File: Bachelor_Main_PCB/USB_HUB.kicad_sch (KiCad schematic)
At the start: 15 parts, among them J11 M20-9990245, U6 USB2514B-I/M2

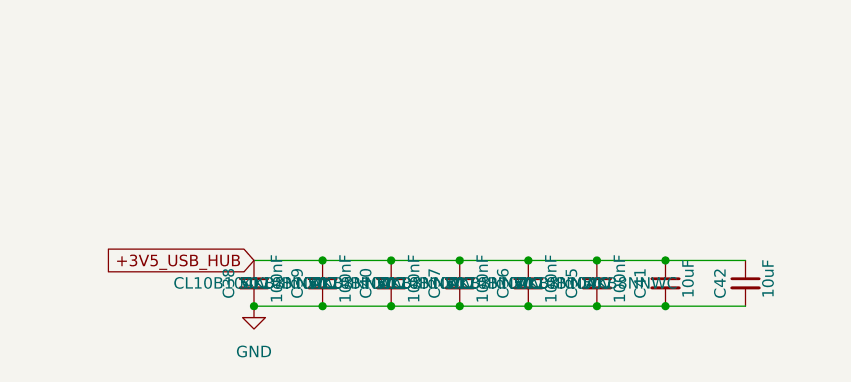
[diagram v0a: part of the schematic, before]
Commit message: Add pulldown to power switch mosfets
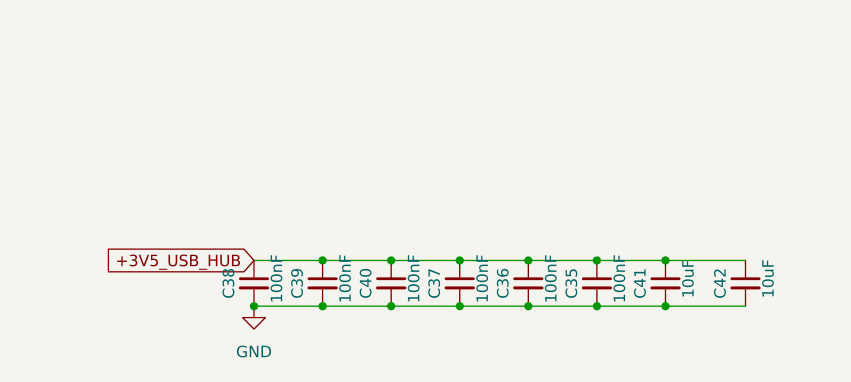
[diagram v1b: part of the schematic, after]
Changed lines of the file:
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@@
 					(size 1.27 1.27)
 				)
+				(hide yes)
 			)
 		)
@@
 					(size 1.27 1.27)
 				)
+				(hide yes)
 			)
 		)
@@
 					(size 1.27 1.27)
 				)
+				(hide yes)
 			)
 		)
@@
 					(size 1.27 1.27)
 				)
+				(hide yes)
 			)
 		)
@@
 					(size 1.27 1.27)
 				)
+				(hide yes)
 			)
 		)
@@
 					(size 1.27 1.27)
 				)
+				(hide yes)
 			)
 		)
@@
 					(size 1.27 1.27)
 				)
+				(hide yes)
 			)
 		)
@@
 					(size 1.27 1.27)
 				)
+				(hide yes)
 			)
 		)
@@
 					(size 1.27 1.27)
 				)
+				(hide yes)
 			)
 		)
@@
 					(size 1.27 1.27)
 				)
+				(hide yes)
 			)
 		)
@@
 					(size 1.27 1.27)
 				)
+				(hide yes)
 			)
 		)
@@
 					(size 1.27 1.27)
 				)
-			)
-		)
+				(hide yes)
+			)
+		)

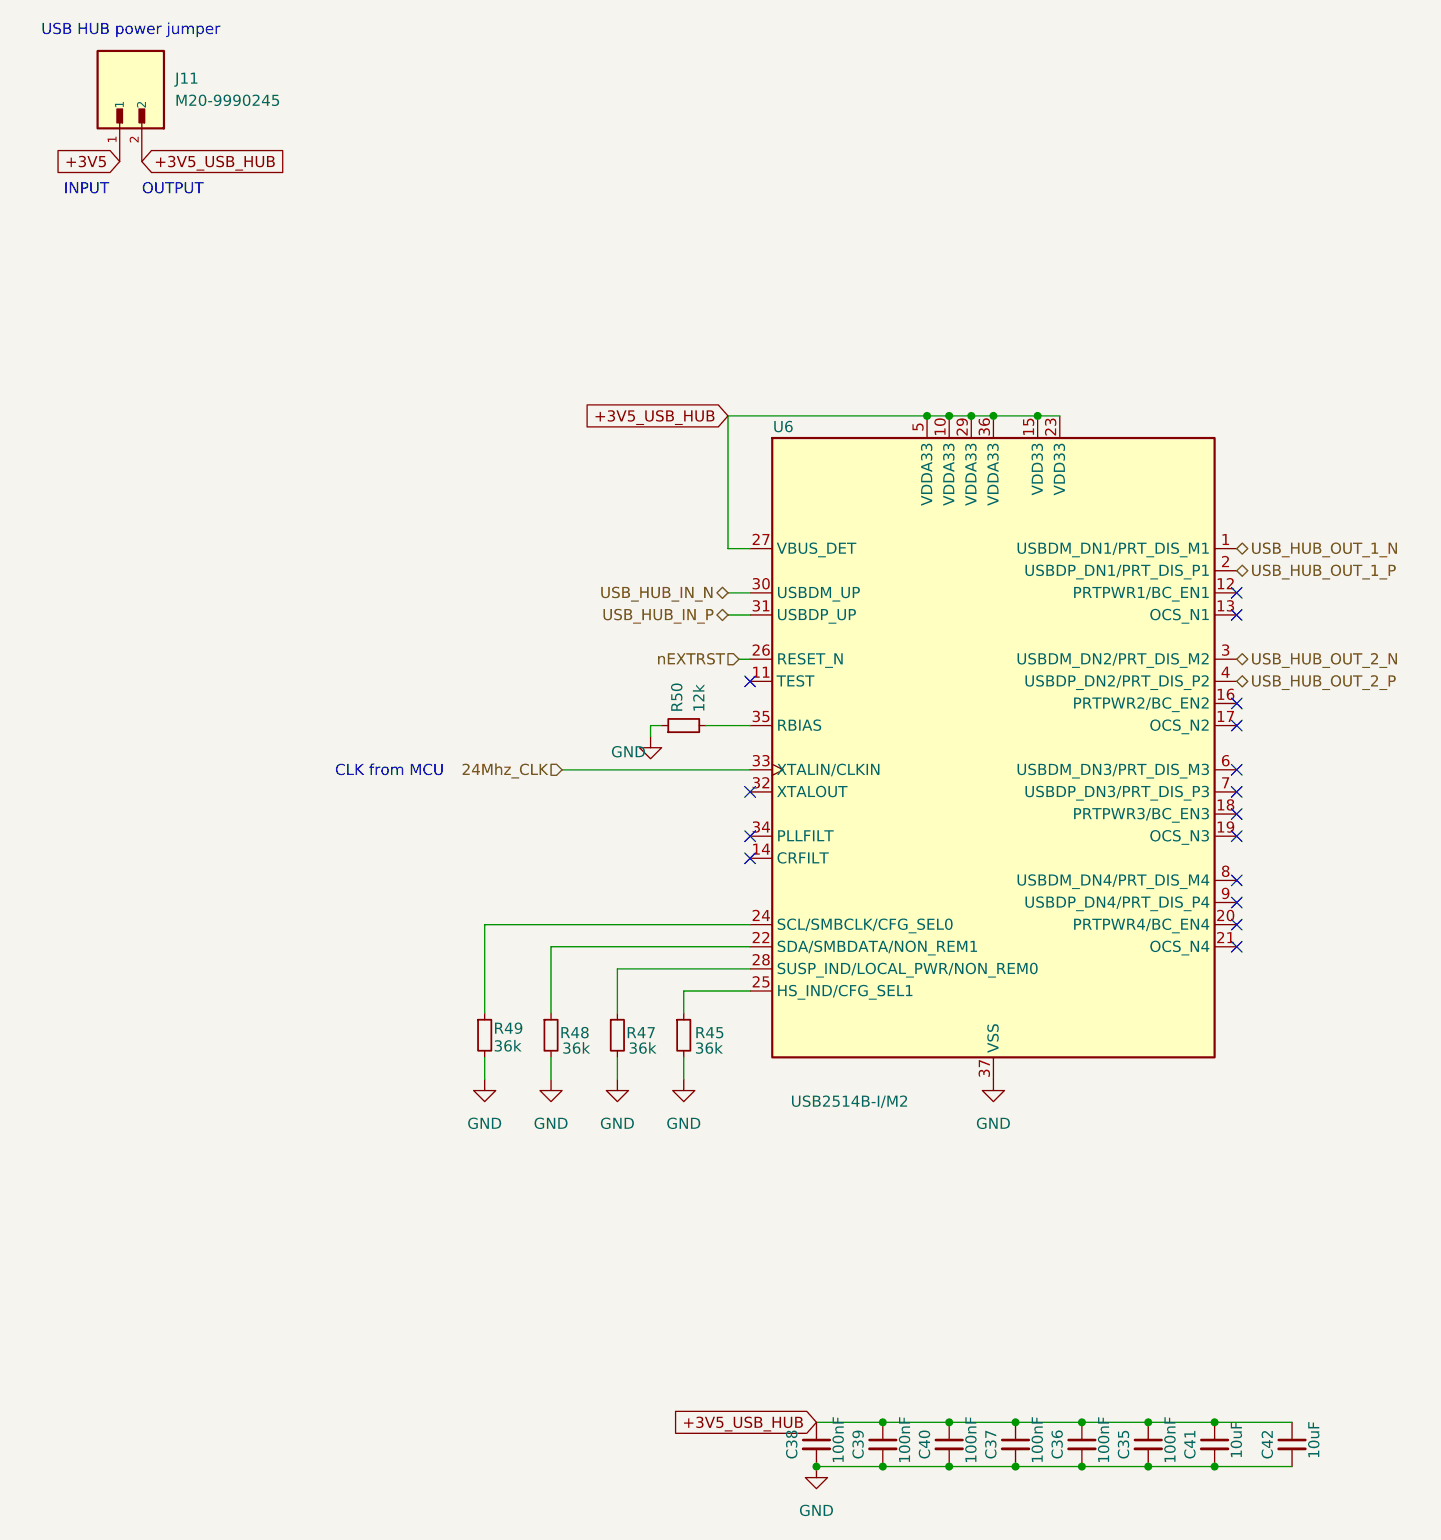
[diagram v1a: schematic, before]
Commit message: Fixed DRC, footprints and power flags and no-connect flags
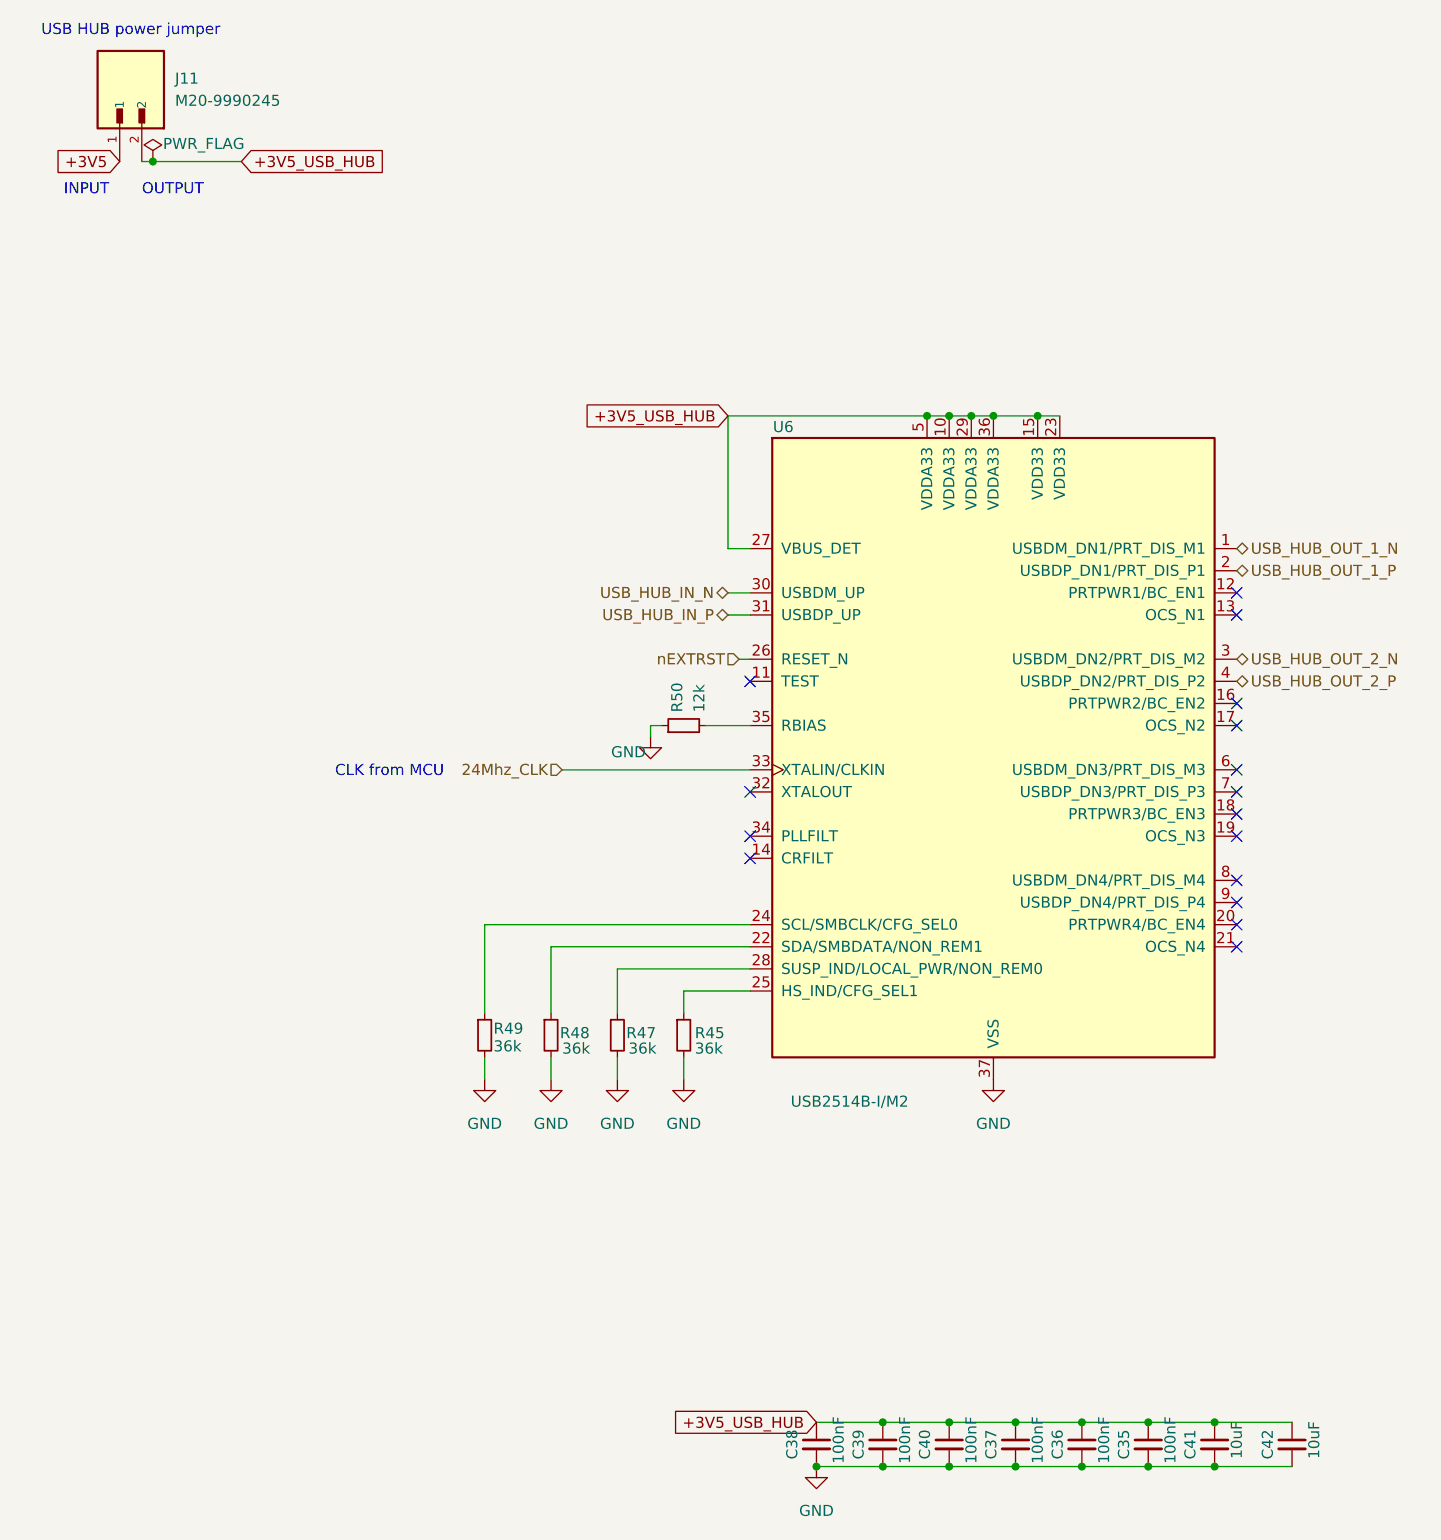
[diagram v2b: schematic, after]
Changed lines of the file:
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@@
+	)
+	(junction
+		(at 34.29 33.02)
+		(diameter 0)
+		(color 0 0 0 0)
 	)
 	(junction
@@
 	(wire
 		(pts
+			(xy 44.45 33.02) (xy 34.29 33.02)
+		)
+		(stroke
+			(width 0)
+			(type default)
+		)
+	)
+	(wire
+		(pts
 			(xy 97.79 97.79) (xy 102.87 97.79)
 		)
@@
 		(pts
 			(xy 110.49 182.88) (xy 118.11 182.88)
+		)
+		(stroke
+			(width 0)
+			(type default)
+		)
+	)
+	(wire
+		(pts
+			(xy 34.29 33.02) (xy 33.02 33.02)
 		)
 		(stroke
@@
 	(global_label "+3V5_USB_HUB"
 		(shape input)
-		(at 33.02 33.02 0)
+		(at 44.45 33.02 0)
 		(fields_autoplaced yes)
 		(effects
@@
 		)
 		(property "Intersheetrefs" "${INTERSHEET_REFS}"
-			(at 50.7008 33.02 0)
+			(at 62.1308 33.02 0)
 			(effects
 				(font
@@
 			)
 		)
-		(property "Description" ""
+		(property "Description" "USB 2.0 Hi-Speed Hub Controller"
 			(at 130.81 100.33 0)
 			(effects
@@
 					(unit 1)
 				)
+			)
+		)
+	)
+	(symbol
+		(lib_id "power:PWR_FLAG")
+		(at 34.29 33.02 0)
+		(unit 1)
+		(exclude_from_sim no)
+		(in_bom yes)
+		(on_board yes)
+		(dnp no)
+		(property "Reference" "#FLG05"
+			(at 34.29 31.115 0)
+			(effects
+				(font
+					(size 1.27 1.27)
+				)
+				(hide yes)
+			)
+		)
+		(property "Value" "PWR_FLAG"
+			(at 40.132 30.988 0)
+			(effects
+				(font
+					(size 1.27 1.27)
+				)
+			)
+		)
+		(property "Footprint" ""
+			(at 34.29 33.02 0)
+			(effects
+				(font
+					(size 1.27 1.27)
+				)
+				(hide yes)
+			)
+		)
+		(property "Datasheet" "~"
+			(at 34.29 33.02 0)
+			(effects
+				(font
+					(size 1.27 1.27)
+				)
+				(hide yes)
+			)
+		)
+		(property "Description" "Special symbol for telling ERC where power comes from"
+			(at 34.29 33.02 0)
+			(effects
+				(font
+					(size 1.27 1.27)
+				)
+				(hide yes)
+			)
+		)
+		(pin "1"
+		)
+		(instances
+			(project "Bachelor_Main_PCB"
+				(path "/3544d663-329e-4884-b753-28436ca187e8/a2efe210-cbe4-4166-b2f4-897451b29d8a"
+					(reference "#FLG05")
+					(unit 1)
+				)

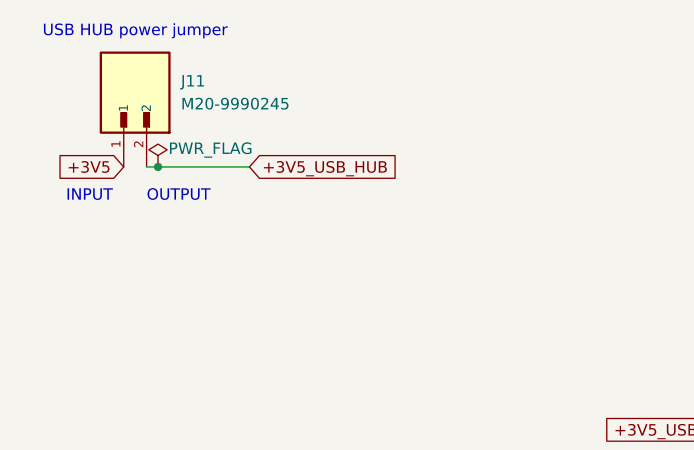
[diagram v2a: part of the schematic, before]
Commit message: Removed Modem_safe_PWR_remove pin.
was potential use for the MCU but would require level shifters and would not add any functionality ass the RPI controls the Modem anyway.
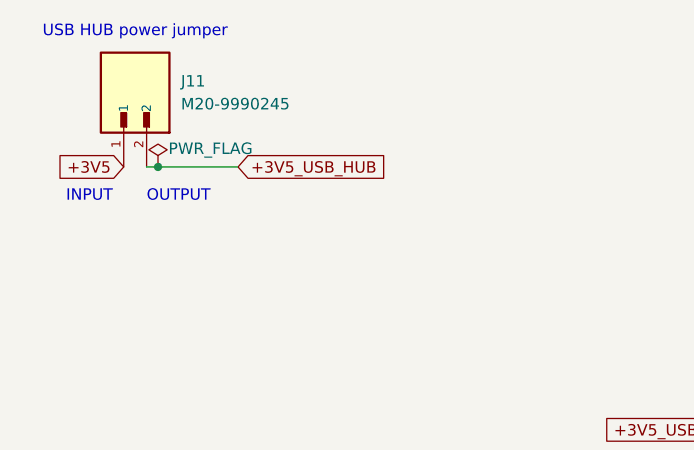
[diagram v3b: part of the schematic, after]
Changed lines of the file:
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@@
 	(wire
 		(pts
-			(xy 44.45 33.02) (xy 34.29 33.02)
+			(xy 43.18 33.02) (xy 34.29 33.02)
 		)
 		(stroke
@@
 	(global_label "+3V5_USB_HUB"
 		(shape input)
-		(at 44.45 33.02 0)
+		(at 43.18 33.02 0)
 		(fields_autoplaced yes)
 		(effects
@@
 		)
 		(property "Intersheetrefs" "${INTERSHEET_REFS}"
-			(at 62.1308 33.02 0)
+			(at 60.8608 33.02 0)
 			(effects
 				(font
